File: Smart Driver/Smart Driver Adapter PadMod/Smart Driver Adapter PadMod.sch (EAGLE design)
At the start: 9 parts, among them U2 DRV8353HMRTATWQFN_HMRTAT_TEX-M

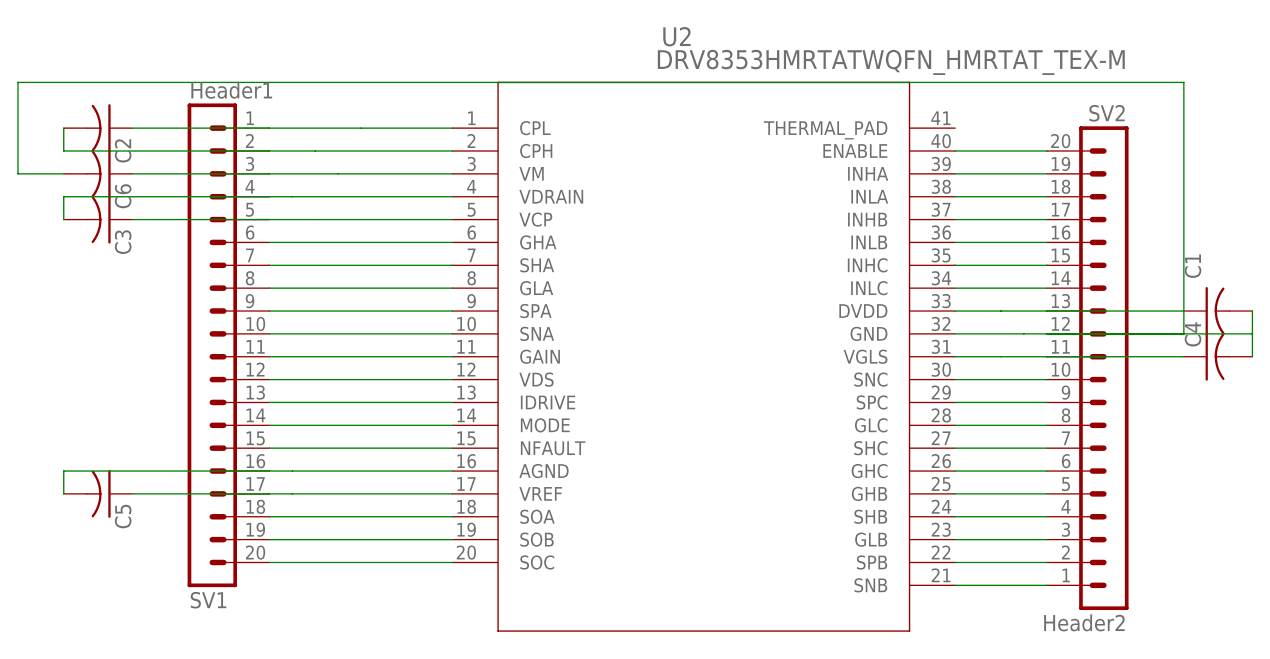
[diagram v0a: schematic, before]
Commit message: Correcting PadMod Version of PCB
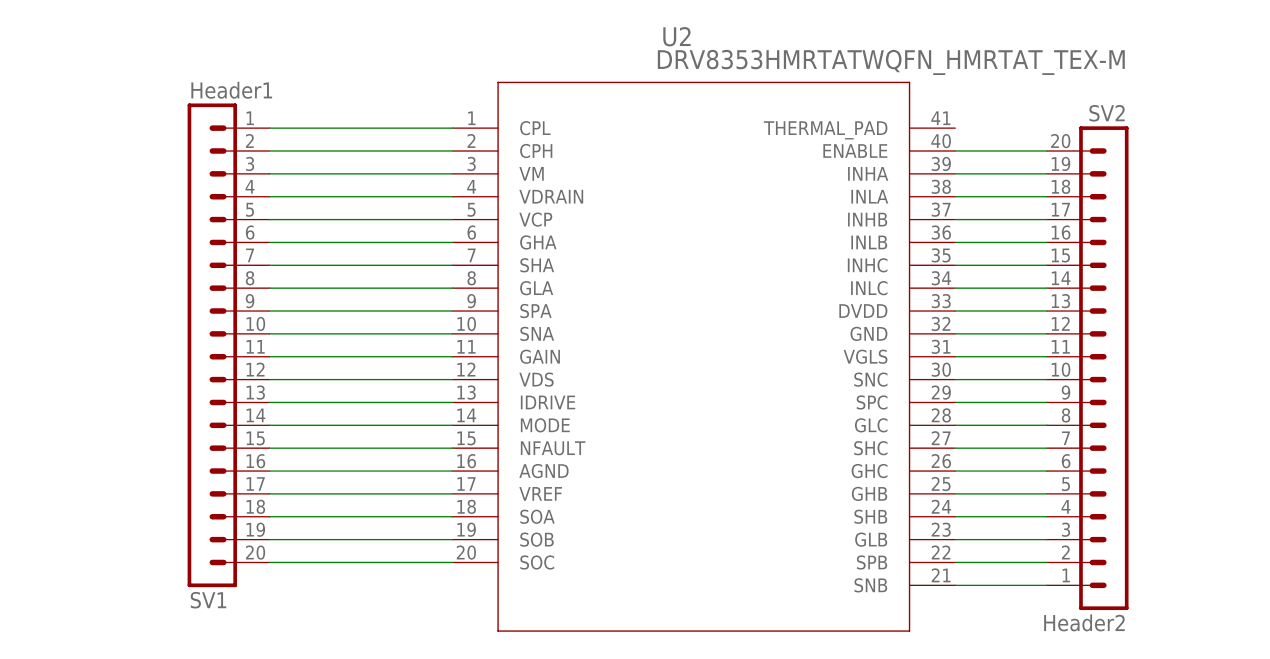
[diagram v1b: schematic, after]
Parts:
- removed C1: (no value), rcl:C-USC0603K
- removed C2, C6: (no value), rcl:C-USC1206K
- removed C3, C4: (no value), rcl:C-USC0805K
- removed C5: (no value), rcl:C-USC0201
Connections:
- removed net N$42: C2.1, SV1.1, U2.CPL
- new net N$26: SV2.13, U2.DVDD
- net N$1: now also SV1.1, U2.CPL; no longer C1.1, SV2.13, U2.DVDD
- net N$15: no longer C5.2
- net N$16: no longer C5.1
- net N$27: no longer C1.2, C4.2, C6.2
- net N$28: no longer C4.1
- net N$3: no longer C2.2
- net N$4: no longer C6.1
- net N$5: no longer C3.2
- net N$6: no longer C3.1
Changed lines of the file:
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@@
 <part name="SV1" library="Modified_Header" deviceset="MA20-1" device="" package3d_urn="urn:adsk.eagle:package:8359/1" value="Header1"/>
 <part name="SV2" library="Modified_Header" deviceset="MA20-1" device="" package3d_urn="urn:adsk.eagle:package:8359/1" value="Header2"/>
-<part name="C1" library="rcl" library_urn="urn:adsk.eagle:library:334" deviceset="C-US" device="C0603K" package3d_urn="urn:adsk.eagle:package:23680/2"/>
-<part name="C2" library="rcl" library_urn="urn:adsk.eagle:library:334" deviceset="C-US" device="C1206K" package3d_urn="urn:adsk.eagle:package:23682/2"/>
-<part name="C3" library="rcl" library_urn="urn:adsk.eagle:library:334" deviceset="C-US" device="C0805K" package3d_urn="urn:adsk.eagle:package:23681/2"/>
-<part name="C4" library="rcl" library_urn="urn:adsk.eagle:library:334" deviceset="C-US" device="C0805K" package3d_urn="urn:adsk.eagle:package:23681/2"/>
-<part name="C5" library="rcl" library_urn="urn:adsk.eagle:library:334" deviceset="C-US" device="C0201" package3d_urn="urn:adsk.eagle:package:23690/2"/>
-<part name="C6" library="rcl" library_urn="urn:adsk.eagle:library:334" deviceset="C-US" device="C1206K" package3d_urn="urn:adsk.eagle:package:23682/2"/>
 </parts>
 <sheets>
@@
 <attribute name="NAME" x="125.73" y="66.802" size="1.778" layer="95" rot="MR0"/>
 </instance>
-<instance part="C1" gate="G$1" x="134.62" y="45.72" smashed="yes" rot="R90">
-<attribute name="NAME" x="133.985" y="49.276" size="1.778" layer="95" rot="R90"/>
-<attribute name="VALUE" x="138.811" y="46.736" size="1.778" layer="96" rot="R90"/>
-</instance>
-<instance part="C2" gate="G$1" x="12.7" y="66.04" smashed="yes" rot="R270">
-<attribute name="NAME" x="13.335" y="65.024" size="1.778" layer="95" rot="R270"/>
-<attribute name="VALUE" x="8.509" y="65.024" size="1.778" layer="96" rot="R270"/>
-</instance>
-<instance part="C3" gate="G$1" x="12.7" y="55.88" smashed="yes" rot="R270">
-<attribute name="NAME" x="13.335" y="54.864" size="1.778" layer="95" rot="R270"/>
-<attribute name="VALUE" x="8.509" y="54.864" size="1.778" layer="96" rot="R270"/>
-</instance>
-<instance part="C4" gate="G$1" x="134.62" y="40.64" smashed="yes" rot="R90">
-<attribute name="NAME" x="133.985" y="41.656" size="1.778" layer="95" rot="R90"/>
-<attribute name="VALUE" x="138.811" y="41.656" size="1.778" layer="96" rot="R90"/>
-</instance>
-<instance part="C5" gate="G$1" x="12.7" y="25.4" smashed="yes" rot="R270">
-<attribute name="NAME" x="13.335" y="24.384" size="1.778" layer="95" rot="R270"/>
-<attribute name="VALUE" x="8.509" y="24.384" size="1.778" layer="96" rot="R270"/>
-</instance>
-<instance part="C6" gate="G$1" x="12.7" y="60.96" smashed="yes" rot="R270">
-<attribute name="NAME" x="13.335" y="59.944" size="1.778" layer="95" rot="R270"/>
-<attribute name="VALUE" x="8.509" y="59.944" size="1.778" layer="96" rot="R270"/>
-</instance>
 </instances>
 <busses>
@@
 <pinref part="SV1" gate="1" pin="3"/>
 <pinref part="U2" gate="A" pin="VM"/>
-<wire x1="30.48" y1="60.96" x2="38.1" y2="60.96" width="0.1524" layer="91"/>
-<pinref part="C6" gate="G$1" pin="1"/>
-<wire x1="38.1" y1="60.96" x2="50.8" y2="60.96" width="0.1524" layer="91"/>
-<wire x1="15.24" y1="60.96" x2="30.48" y2="60.96" width="0.1524" layer="91"/>
+<wire x1="30.48" y1="60.96" x2="50.8" y2="60.96" width="0.1524" layer="91"/>
 </segment>
 </net>
@@
 <pinref part="U2" gate="A" pin="VDRAIN"/>
 <pinref part="SV1" gate="1" pin="4"/>
-<wire x1="50.8" y1="58.42" x2="33.02" y2="58.42" width="0.1524" layer="91"/>
-<pinref part="C3" gate="G$1" pin="2"/>
-<wire x1="33.02" y1="58.42" x2="30.48" y2="58.42" width="0.1524" layer="91"/>
-<wire x1="7.62" y1="55.88" x2="7.62" y2="58.42" width="0.1524" layer="91"/>
-<wire x1="7.62" y1="58.42" x2="30.48" y2="58.42" width="0.1524" layer="91"/>
+<wire x1="50.8" y1="58.42" x2="30.48" y2="58.42" width="0.1524" layer="91"/>
 </segment>
 </net>
@@
 <pinref part="SV1" gate="1" pin="5"/>
 <pinref part="U2" gate="A" pin="VCP"/>
-<wire x1="30.48" y1="55.88" x2="35.56" y2="55.88" width="0.1524" layer="91"/>
-<pinref part="C3" gate="G$1" pin="1"/>
-<wire x1="35.56" y1="55.88" x2="50.8" y2="55.88" width="0.1524" layer="91"/>
-<wire x1="15.24" y1="55.88" x2="30.48" y2="55.88" width="0.1524" layer="91"/>
+<wire x1="30.48" y1="55.88" x2="50.8" y2="55.88" width="0.1524" layer="91"/>
 </segment>
 </net>
@@
 <pinref part="SV1" gate="1" pin="16"/>
 <pinref part="U2" gate="A" pin="AGND"/>
-<wire x1="30.48" y1="27.94" x2="33.02" y2="27.94" width="0.1524" layer="91"/>
-<pinref part="C5" gate="G$1" pin="2"/>
-<wire x1="33.02" y1="27.94" x2="50.8" y2="27.94" width="0.1524" layer="91"/>
-<wire x1="7.62" y1="25.4" x2="7.62" y2="27.94" width="0.1524" layer="91"/>
-<wire x1="7.62" y1="27.94" x2="30.48" y2="27.94" width="0.1524" layer="91"/>
+<wire x1="30.48" y1="27.94" x2="50.8" y2="27.94" width="0.1524" layer="91"/>
 </segment>
 </net>
@@
 <pinref part="U2" gate="A" pin="VREF"/>
 <pinref part="SV1" gate="1" pin="17"/>
-<wire x1="50.8" y1="25.4" x2="33.02" y2="25.4" width="0.1524" layer="91"/>
-<pinref part="C5" gate="G$1" pin="1"/>
-<wire x1="33.02" y1="25.4" x2="30.48" y2="25.4" width="0.1524" layer="91"/>
-<wire x1="15.24" y1="25.4" x2="30.48" y2="25.4" width="0.1524" layer="91"/>
+<wire x1="50.8" y1="25.4" x2="30.48" y2="25.4" width="0.1524" layer="91"/>
 </segment>
 </net>
@@
 </segment>
 </net>
+<net name="N$26" class="0">
+<segment>
+<pinref part="SV2" gate="1" pin="13"/>
+<pinref part="U2" gate="A" pin="DVDD"/>
+<wire x1="116.84" y1="45.72" x2="106.68" y2="45.72" width="0.1524" layer="91"/>
+</segment>
+</net>
 <net name="N$27" class="0">
 <segment>
 <pinref part="U2" gate="A" pin="GND"/>
 <pinref part="SV2" gate="1" pin="12"/>
-<wire x1="106.68" y1="43.18" x2="114.3" y2="43.18" width="0.1524" layer="91"/>
-<pinref part="C1" gate="G$1" pin="2"/>
-<wire x1="139.7" y1="45.72" x2="139.7" y2="43.18" width="0.1524" layer="91"/>
-<wire x1="139.7" y1="43.18" x2="116.84" y2="43.18" width="0.1524" layer="91"/>
-<pinref part="C4" gate="G$1" pin="2"/>
-<wire x1="139.7" y1="40.64" x2="139.7" y2="43.18" width="0.1524" layer="91"/>
-<pinref part="C6" gate="G$1" pin="2"/>
-<wire x1="7.62" y1="60.96" x2="2.54" y2="60.96" width="0.1524" layer="91"/>
-<wire x1="2.54" y1="60.96" x2="2.54" y2="71.12" width="0.1524" layer="91"/>
-<wire x1="2.54" y1="71.12" x2="132.08" y2="71.12" width="0.1524" layer="91"/>
-<wire x1="132.08" y1="71.12" x2="132.08" y2="43.18" width="0.1524" layer="91"/>
-<wire x1="132.08" y1="43.18" x2="114.3" y2="43.18" width="0.1524" layer="91"/>
+<wire x1="106.68" y1="43.18" x2="116.84" y2="43.18" width="0.1524" layer="91"/>
 </segment>
 </net>
@@
 <pinref part="SV2" gate="1" pin="11"/>
 <pinref part="U2" gate="A" pin="VGLS"/>
-<wire x1="116.84" y1="40.64" x2="111.76" y2="40.64" width="0.1524" layer="91"/>
-<pinref part="C4" gate="G$1" pin="1"/>
-<wire x1="111.76" y1="40.64" x2="106.68" y2="40.64" width="0.1524" layer="91"/>
-<wire x1="132.08" y1="40.64" x2="116.84" y2="40.64" width="0.1524" layer="91"/>
+<wire x1="116.84" y1="40.64" x2="106.68" y2="40.64" width="0.1524" layer="91"/>
 </segment>
 </net>
@@
 </segment>
 </net>
+<net name="N$1" class="0">
+<segment>
+<pinref part="SV1" gate="1" pin="1"/>
+<pinref part="U2" gate="A" pin="CPL"/>
+<wire x1="30.48" y1="66.04" x2="50.8" y2="66.04" width="0.1524" layer="91"/>
+</segment>
+</net>
 <net name="N$3" class="0">
 <segment>
 <pinref part="U2" gate="A" pin="CPH"/>
 <pinref part="SV1" gate="1" pin="2"/>
-<wire x1="50.8" y1="63.5" x2="35.56" y2="63.5" width="0.1524" layer="91"/>
-<pinref part="C2" gate="G$1" pin="2"/>
-<wire x1="35.56" y1="63.5" x2="30.48" y2="63.5" width="0.1524" layer="91"/>
-<wire x1="7.62" y1="66.04" x2="7.62" y2="63.5" width="0.1524" layer="91"/>
-<wire x1="7.62" y1="63.5" x2="30.48" y2="63.5" width="0.1524" layer="91"/>
+<wire x1="50.8" y1="63.5" x2="30.48" y2="63.5" width="0.1524" layer="91"/>
 </segment>
 </net>
@@
 <pinref part="U2" gate="A" pin="SOB"/>
 <wire x1="30.48" y1="20.32" x2="50.8" y2="20.32" width="0.1524" layer="91"/>
-</segment>
-</net>
-<net name="N$42" class="0">
-<segment>
-<pinref part="U2" gate="A" pin="CPL"/>
-<pinref part="SV1" gate="1" pin="1"/>
-<wire x1="30.48" y1="66.04" x2="40.64" y2="66.04" width="0.1524" layer="91"/>
-<pinref part="C2" gate="G$1" pin="1"/>
-<wire x1="40.64" y1="66.04" x2="50.8" y2="66.04" width="0.1524" layer="91"/>
-<wire x1="15.24" y1="66.04" x2="30.48" y2="66.04" width="0.1524" layer="91"/>
-</segment>
-</net>
-<net name="N$1" class="0">
-<segment>
-<pinref part="U2" gate="A" pin="DVDD"/>
-<pinref part="SV2" gate="1" pin="13"/>
-<wire x1="116.84" y1="45.72" x2="111.76" y2="45.72" width="0.1524" layer="91"/>
-<pinref part="C1" gate="G$1" pin="1"/>
-<wire x1="111.76" y1="45.72" x2="106.68" y2="45.72" width="0.1524" layer="91"/>
-<wire x1="132.08" y1="45.72" x2="116.84" y2="45.72" width="0.1524" layer="91"/>
 </segment>
 </net>
@@
 </drawing>
 <compatibility>
-<note version="8.2" severity="warning">
-Since Version 8.2, EAGLE supports online libraries. The ids
-of those online libraries will not be understood (or retained)
-with this version.
-</note>
 <note version="8.3" severity="warning">
 Since Version 8.3, EAGLE supports URNs for individual library
@@
 packages will not be understood (or retained) with this version.
 </note>
-<note version="8.4" severity="warning">
-Since Version 8.4, EAGLE supports properties for SPICE simulation.
-Probes in schematics and SPICE mapping objects found in parts and library devices
-will not be understood with this version. Update EAGLE to the latest version
-for full support of SPICE simulation.
-</note>
 </compatibility>
